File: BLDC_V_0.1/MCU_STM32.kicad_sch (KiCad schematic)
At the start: 32 parts, among them J2 SWD, J3 Conn_01x03, J4 Conn_01x04, J5 USB_B_Micro, U3 AMS1117, U3 USBLC6-2SC6, U5 STM32G473VET6, Y1 24MHz

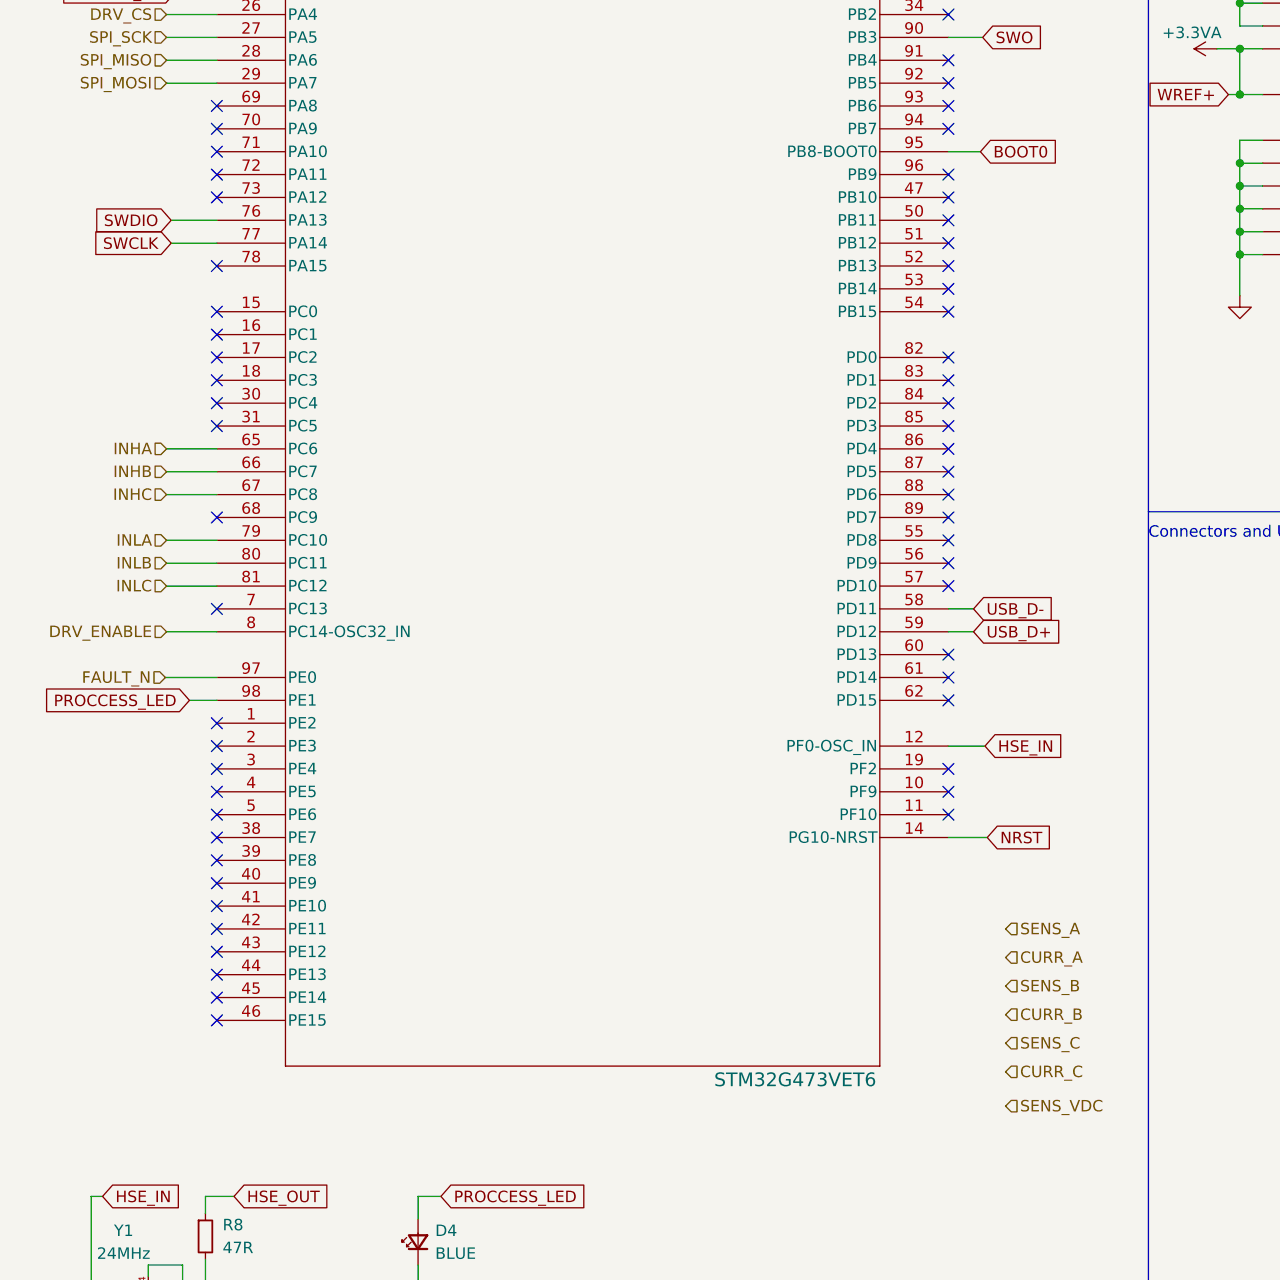
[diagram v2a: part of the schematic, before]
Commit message: MCU ADC allocation is done.
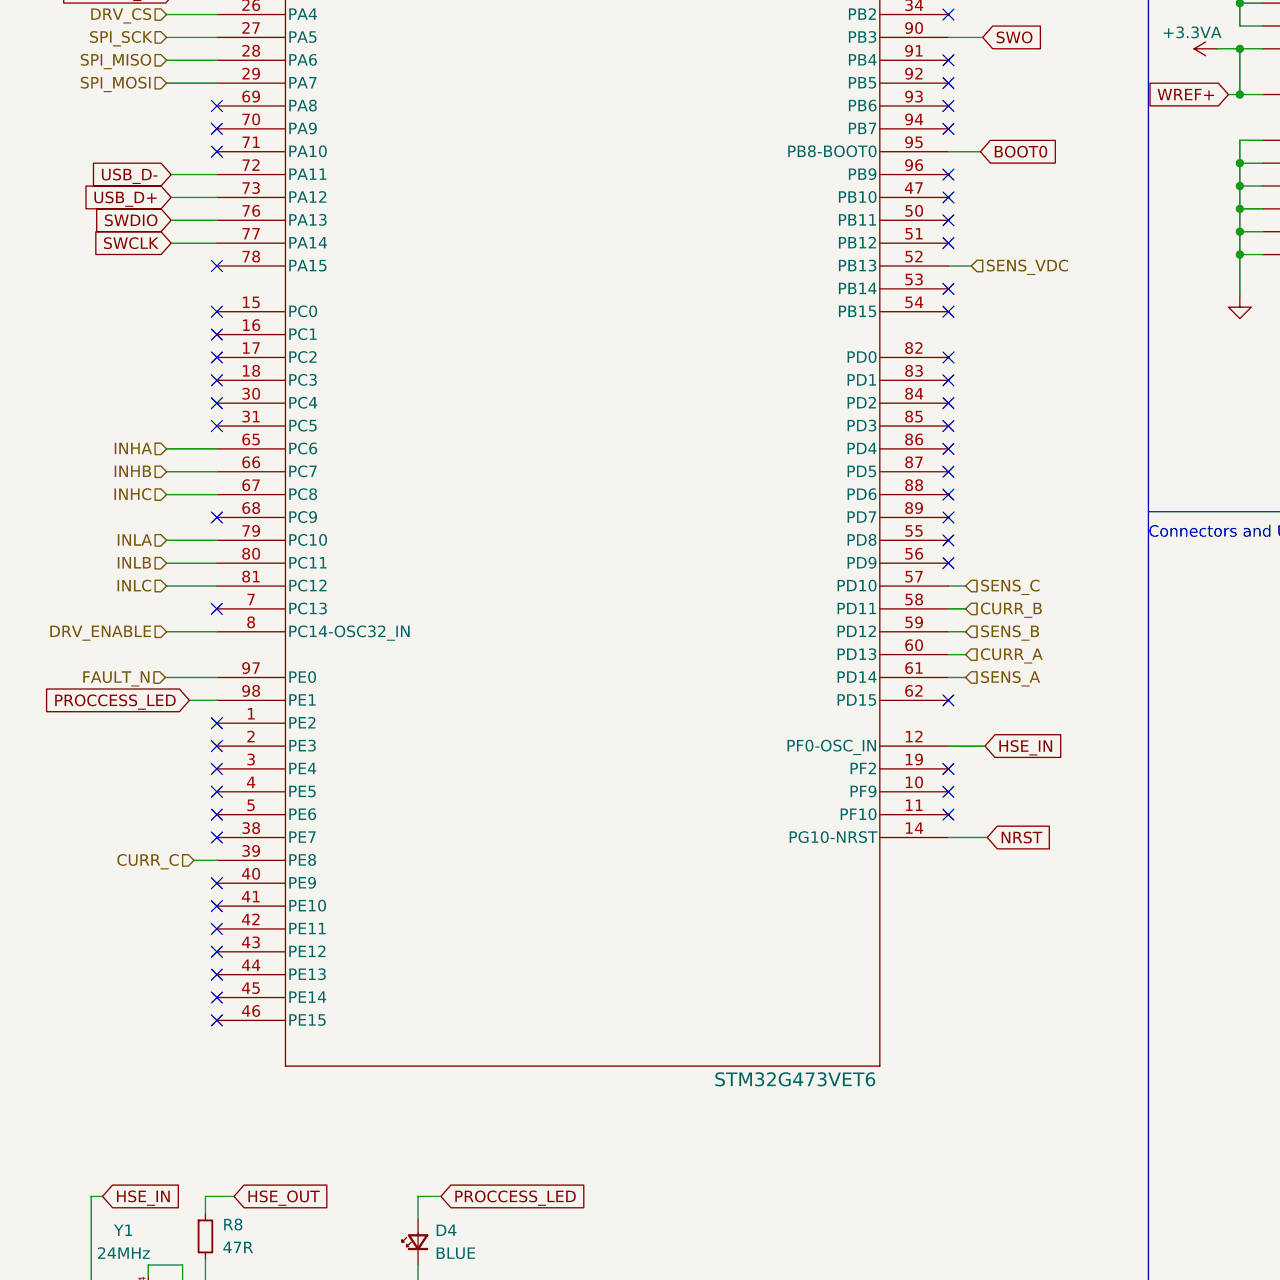
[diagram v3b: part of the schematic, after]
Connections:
- net CURR_A: now also U5.60 (PD13)
- net CURR_B: now also U5.58 (PD11)
- net CURR_C: now also U5.39 (PE8)
- net SENS_A: now also U5.61 (PD14)
- net SENS_B: now also U5.59 (PD12)
- net SENS_C: now also U5.57 (PD10)
- net SENS_VDC: now also U5.52 (PB13)
- net USB_D+: now also U5.73 (PA12); no longer U5.59 (PD12)
- net USB_D-: now also U5.72 (PA11); no longer U5.58 (PD11)
- no-connect marks 66 -> 59
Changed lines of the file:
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@@
   (no_connect (at 114.3 35.56))
   (no_connect (at 114.3 71.12))
-  (no_connect (at 114.3 111.76))
   (no_connect (at 114.3 48.26))
   (no_connect (at 33.02 132.08))
@@
   (no_connect (at 114.3 99.06))
   (no_connect (at 33.02 119.38))
+  (no_connect (at 114.3 116.84))
   (no_connect (at 114.3 27.94))
   (no_connect (at 114.3 101.6))
@@
   (no_connect (at 114.3 50.8))
   (no_connect (at 33.02 76.2))
-  (no_connect (at 33.02 58.42))
   (no_connect (at 114.3 73.66))
   (no_connect (at 114.3 93.98))
@@
   (no_connect (at 114.3 127))
   (no_connect (at 114.3 96.52))
-  (no_connect (at 114.3 116.84))
   (no_connect (at 114.3 63.5))
   (no_connect (at 182.88 147.955))
-  (no_connect (at 33.02 60.96))
   (no_connect (at 114.3 60.96))
   (no_connect (at 33.02 121.92))
@@
   (no_connect (at 33.02 139.7))
   (no_connect (at 33.02 127))
-  (no_connect (at 114.3 68.58))
   (no_connect (at 33.02 68.58))
   (no_connect (at 33.02 50.8))
@@
   (no_connect (at 33.02 53.34))
   (no_connect (at 33.02 81.28))
-  (no_connect (at 33.02 134.62))
   (no_connect (at 114.3 83.82))
-  (no_connect (at 114.3 114.3))
   (no_connect (at 114.3 91.44))
   (no_connect (at 114.3 86.36))
@@
   (no_connect (at 170.18 147.955))
   (no_connect (at 33.02 33.02))
-  (no_connect (at 114.3 104.14))
   (no_connect (at 114.3 78.74))
   (wire (pts (xy 57.912 171.958) (xy 55.372 171.958))
@@
     (stroke (width 0) (type default))
   )
+  (wire (pts (xy 114.3 68.58) (xy 116.84 68.58))
+    (stroke (width 0) (type default))
+  )
   (wire (pts (xy 146.685 64.77) (xy 146.685 67.31))
     (stroke (width 0) (type default))
@@
     (stroke (width 0) (type default))
   )
+  (wire (pts (xy 27.94 60.96) (xy 33.02 60.96))
+    (stroke (width 0) (type default))
+  )
   (wire (pts (xy 234.315 66.675) (xy 234.315 65.405))
     (stroke (width 0) (type default))
@@
     (stroke (width 0) (type default))
   )
+  (wire (pts (xy 114.3 114.3) (xy 116.205 114.3))
+    (stroke (width 0) (type default))
+  )
   (polyline (pts (xy 136.525 12.192) (xy 136.525 95.885))
     (stroke (width 0) (type default))
@@
     (stroke (width 0) (type default))
   )
-  (wire (pts (xy 114.3 109.22) (xy 117.094 109.22))
-    (stroke (width 0) (type default))
-  )
   (wire (pts (xy 168.275 145.415) (xy 168.275 150.495))
     (stroke (width 0) (type default))
   )
+  (wire (pts (xy 114.3 106.68) (xy 116.205 106.68))
+    (stroke (width 0) (type default))
+  )
   (wire (pts (xy 25.4 192.913) (xy 31.75 192.913))
     (stroke (width 0) (type default))
@@
     (stroke (width 0) (type default))
   )
+  (wire (pts (xy 114.3 109.22) (xy 116.205 109.22))
+    (stroke (width 0) (type default))
+  )
   (wire (pts (xy 31.75 187.198) (xy 31.75 183.388))
     (stroke (width 0) (type default))
@@
     (stroke (width 0) (type default))
   )
-  (wire (pts (xy 114.3 106.68) (xy 117.094 106.68))
-    (stroke (width 0) (type default))
-  )
   (wire (pts (xy 254 22.606) (xy 254 28.956))
     (stroke (width 0) (type default))
@@
     (stroke (width 0) (type default))
   )
+  (wire (pts (xy 27.94 58.42) (xy 33.02 58.42))
+    (stroke (width 0) (type default))
+  )
   (wire (pts (xy 250.571 54.61) (xy 250.571 53.975))
     (stroke (width 0) (type default))
@@
     (stroke (width 0) (type default))
   )
+  (wire (pts (xy 30.48 134.62) (xy 33.02 134.62))
+    (stroke (width 0) (type default))
+  )
   (wire (pts (xy 28.448 38.1) (xy 33.02 38.1))
     (stroke (width 0) (type default))
@@
     (stroke (width 0) (type default))
   )
+  (wire (pts (xy 114.3 111.76) (xy 116.205 111.76))
+    (stroke (width 0) (type default))
+  )
   (wire (pts (xy 195.58 144.145) (xy 196.85 144.145))
     (stroke (width 0) (type default))
@@
   )
   (wire (pts (xy 25.4 193.548) (xy 25.4 192.913))
+    (stroke (width 0) (type default))
+  )
+  (wire (pts (xy 114.3 104.14) (xy 116.205 104.14))
     (stroke (width 0) (type default))
   )
@@
     )
   )
-  (global_label "USB_D+" (shape input) (at 117.094 109.22 0)
-    (effects (font (size 1.27 1.27)) (justify left))
-    (property "Intersheetrefs" "${INTERSHEET_REFS}" (at 117.094 109.22 0)
+  (global_label "USB_D+" (shape input) (at 27.94 60.96 180)
+    (effects (font (size 1.27 1.27)) (justify right))
+    (property "Intersheetrefs" "${INTERSHEET_REFS}" (at 27.94 60.96 0)
       (effects (font (size 1.27 1.27)) hide)
     )
@@
     )
   )
-  (global_label "USB_D-" (shape input) (at 117.094 106.68 0)
-    (effects (font (size 1.27 1.27)) (justify left))
-    (property "Intersheetrefs" "${INTERSHEET_REFS}" (at 117.094 106.68 0)
+  (global_label "USB_D-" (shape input) (at 27.94 58.42 180)
+    (effects (font (size 1.27 1.27)) (justify right))
+    (property "Intersheetrefs" "${INTERSHEET_REFS}" (at 27.94 58.42 0)
       (effects (font (size 1.27 1.27)) hide)
     )
@@
     (effects (font (size 1.27 1.27)) (justify right))
   )
-  (hierarchical_label "CURR_A" (shape input) (at 120.65 145.415 0) (fields_autoplaced)
+  (hierarchical_label "CURR_A" (shape input) (at 116.205 111.76 0) (fields_autoplaced)
     (effects (font (size 1.27 1.27)) (justify left))
   )
@@
     (effects (font (size 1.27 1.27)) (justify right))
   )
-  (hierarchical_label "SENS_B" (shape input) (at 120.65 148.59 0) (fields_autoplaced)
+  (hierarchical_label "SENS_B" (shape input) (at 116.205 109.22 0) (fields_autoplaced)
     (effects (font (size 1.27 1.27)) (justify left))
   )
@@
     (effects (font (size 1.27 1.27)) (justify right))
   )
-  (hierarchical_label "SENS_VDC" (shape input) (at 120.65 161.925 0) (fields_autoplaced)
+  (hierarchical_label "SENS_VDC" (shape input) (at 116.84 68.58 0) (fields_autoplaced)
     (effects (font (size 1.27 1.27)) (justify left))
   )
@@
     (effects (font (size 1.27 1.27)) (justify right))
   )
-  (hierarchical_label "SENS_A" (shape input) (at 120.65 142.24 0) (fields_autoplaced)
-    (effects (font (size 1.27 1.27)) (justify left))
-  )
-  (hierarchical_label "CURR_C" (shape input) (at 120.65 158.115 0) (fields_autoplaced)
-    (effects (font (size 1.27 1.27)) (justify left))
+  (hierarchical_label "SENS_A" (shape input) (at 116.205 114.3 0) (fields_autoplaced)
+    (effects (font (size 1.27 1.27)) (justify left))
+  )
+  (hierarchical_label "CURR_C" (shape input) (at 30.48 134.62 180) (fields_autoplaced)
+    (effects (font (size 1.27 1.27)) (justify right))
   )
   (hierarchical_label "DRV_CS" (shape input) (at 27.432 40.64 180) (fields_autoplaced)
@@
     (effects (font (size 1.27 1.27)) (justify right))
   )
-  (hierarchical_label "CURR_B" (shape input) (at 120.65 151.765 0) (fields_autoplaced)
-    (effects (font (size 1.27 1.27)) (justify left))
-  )
-  (hierarchical_label "SENS_C" (shape input) (at 120.65 154.94 0) (fields_autoplaced)
-    (effects (font (size 1.27 1.27)) (justify left))
-  )
+  (hierarchical_label "CURR_B" (shape input) (at 116.205 106.68 0) (fields_autoplaced)
+    (effects (font (size 1.27 1.27)) (justify left))
+  )
+  (hierarchical_label "SENS_C" (shape input) (at 116.205 104.14 0) (fields_autoplaced)
+    (effects (font (size 1.27 1.27)) (justify left))
+  )

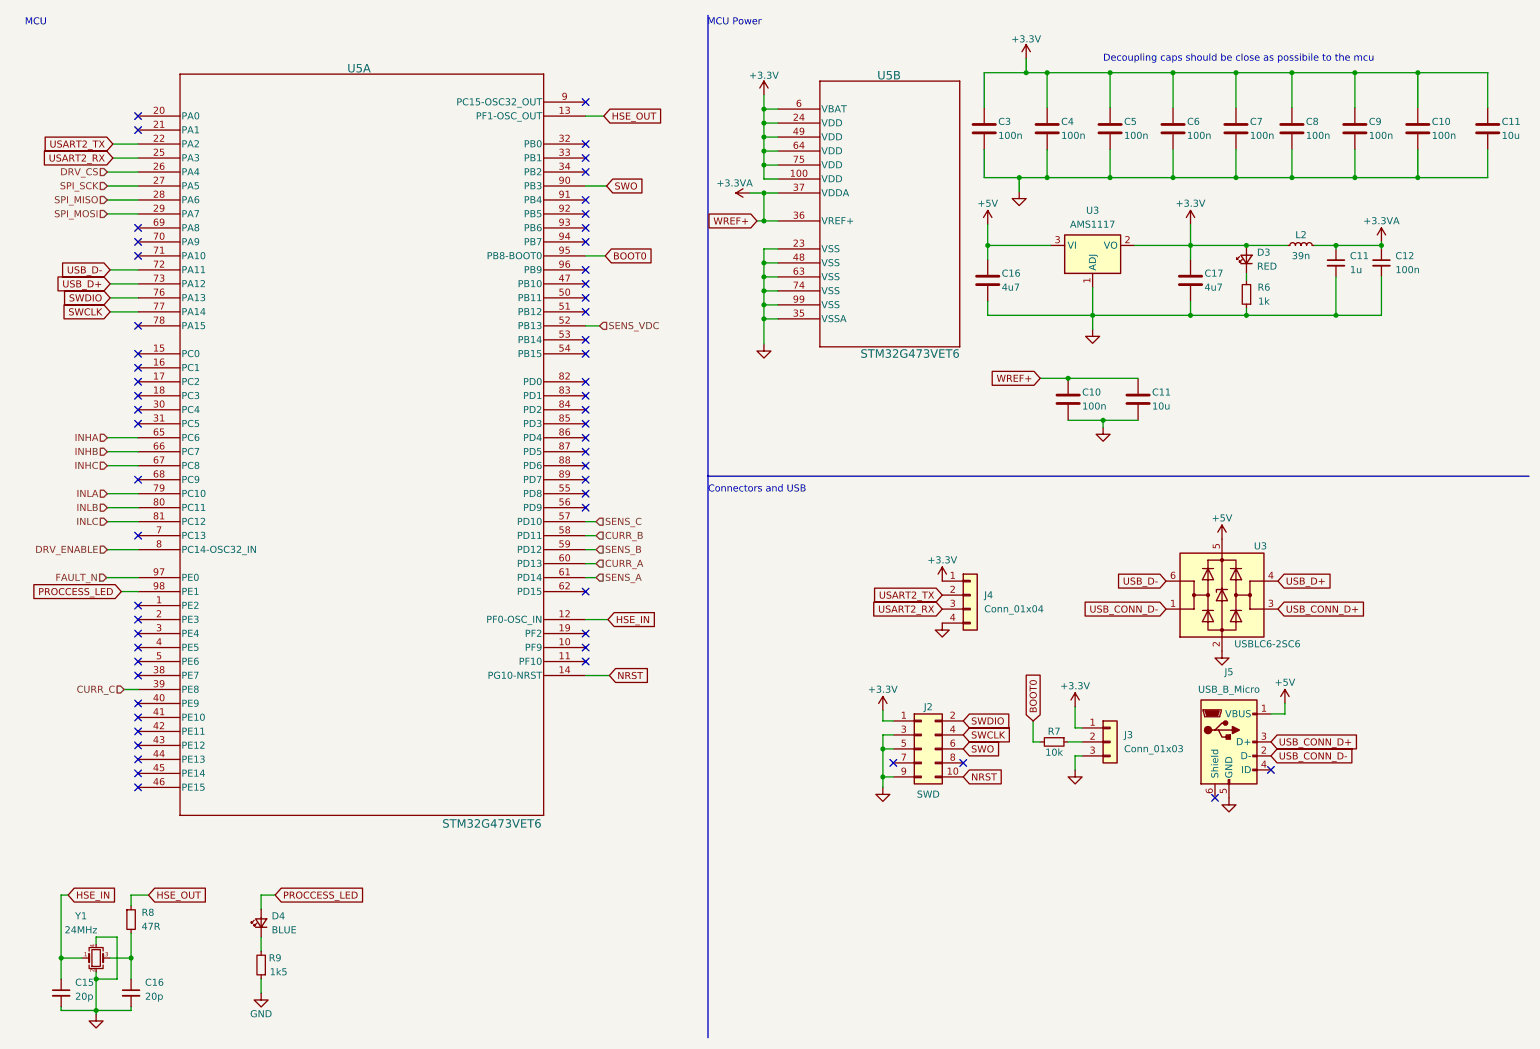
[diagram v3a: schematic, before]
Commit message: Connectors and CAN circuit added.
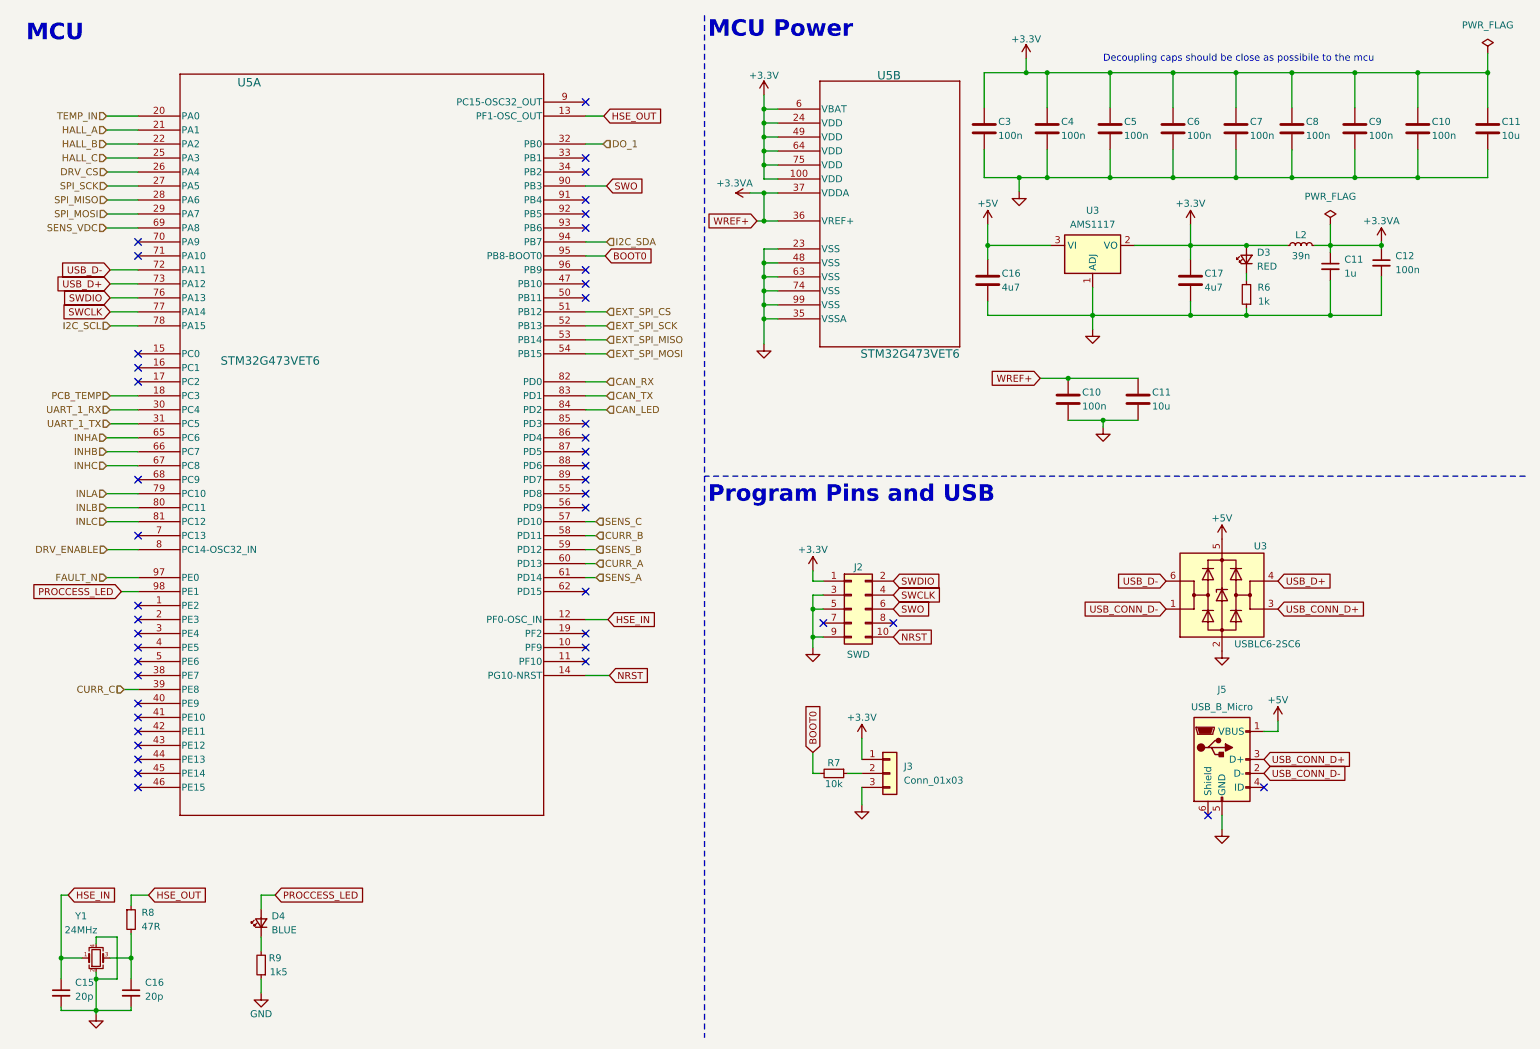
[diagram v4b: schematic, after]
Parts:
- removed J4: Conn_01x04, Connector_Molex:Molex_PicoBlade_53048-0410_1x04_P1.25mm_Horizontal, symbol Connector_Generic:Conn_01x04
- C3: footprint (none) -> Capacitor_SMD:C_0402_1005Metric
- D3, D4: footprint (none) -> LED_SMD:LED_0805_2012Metric
- J3: footprint (none) -> Connector:FanPinHeader_1x03_P2.54mm_Vertical
- J5: footprint (none) -> Connector_USB:USB_Micro-AB_Molex_47590-0001; Link (none) -> https://jlcpcb.com/partdetail/Molex-475900001/C136001
- L2: footprint (none) -> 15EDGVC:CONN_15EDGVC-3.5-03P-1X_DEG
- R6, R9: footprint (none) -> Resistor_SMD:R_0402_1005Metric
- U3: footprint (none) -> Package_TO_SOT_SMD:SOT-23-6
- U5: footprint LQFP100-14x14mm -> STM32G473VET6:LQFP100-14x14mm
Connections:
- net SENS_VDC: now also U5.69 (PA8); no longer U5.52 (PB13)
- net PCB_TEMP: now reaches U5.18 (PC3)
- net TEMP_IN: now reaches U5.20 (PA0)
- net HALL_A: now reaches U5.21 (PA1)
- net UART_1_RX: now reaches U5.30 (PC4)
- net UART_1_TX: now reaches U5.31 (PC5)
- net DO_1: now reaches U5.32 (PB0)
- net EXT_SPI_CS: now reaches U5.51 (PB12)
- net EXT_SPI_MISO: now reaches U5.53 (PB14)
- net EXT_SPI_MOSI: now reaches U5.54 (PB15)
- net I2C_SCL: now reaches U5.78 (PA15)
- net CAN_RX: now reaches U5.82 (PD0)
- net CAN_TX: now reaches U5.83 (PD1)
- net CAN_LED: now reaches U5.84 (PD2)
- net I2C_SDA: now reaches U5.94 (PB7)
- net USART2_RX renamed HALL_C
- net USART2_TX renamed HALL_B
- new net EXT_SPI_SCK: U5.52 (PB13)
- no-connect marks 59 -> 44
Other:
- note added: "Program Pins and USB"
- note removed: "Connectors and USB"
- moved on the sheet: C11, J2, J3, J5, R7
